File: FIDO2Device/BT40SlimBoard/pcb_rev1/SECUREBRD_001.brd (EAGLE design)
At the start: 30 x 30 mm, 31 parts, among them CN1 2137160001, CN2 IF_5PIN_H, CN3 IF_4PIN_SOL, SW1 SKRPACE010, SW2 SKRPACE010, SW3 SKTADAE010, U1 BT40, U2 ADP122ACPZ-3.3-R7

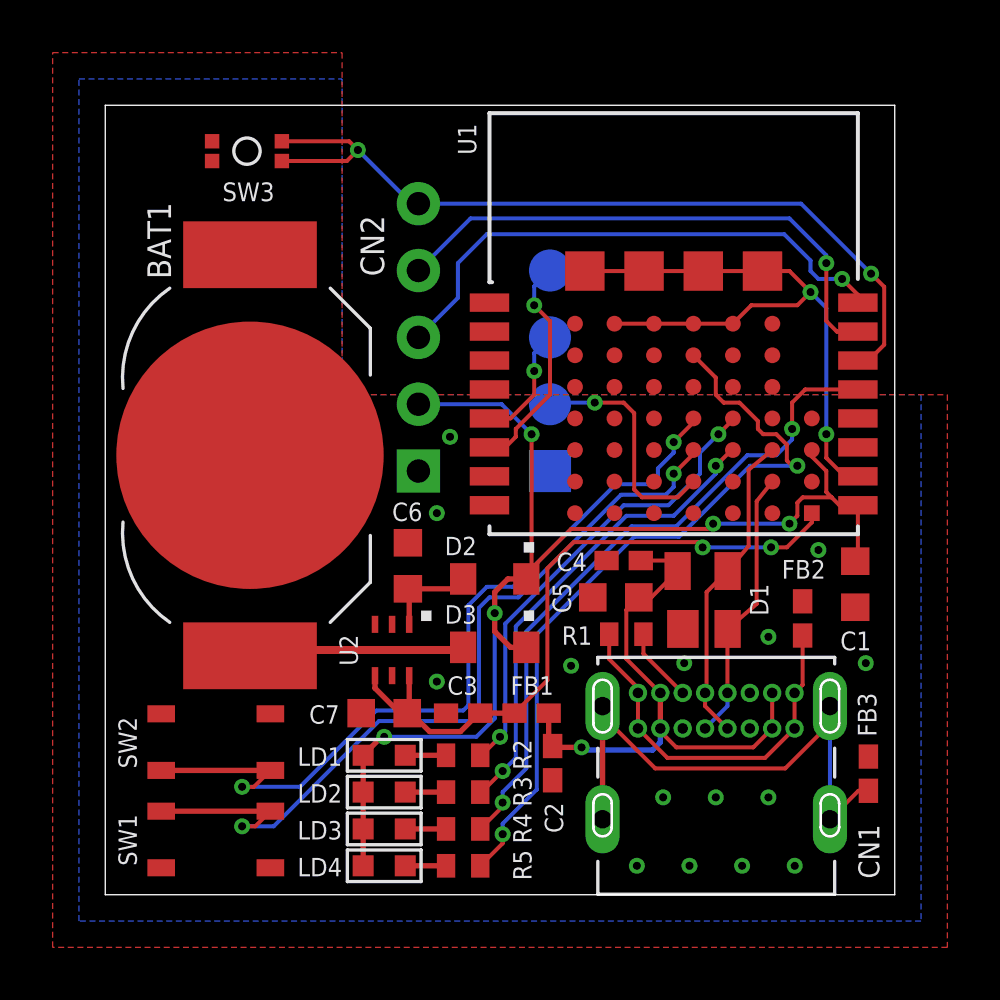
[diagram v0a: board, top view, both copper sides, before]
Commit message: パターンの改善
・裏面べたGNDの狭かった経路部分を拡張
（スイッチ、LEDのviaを改善）
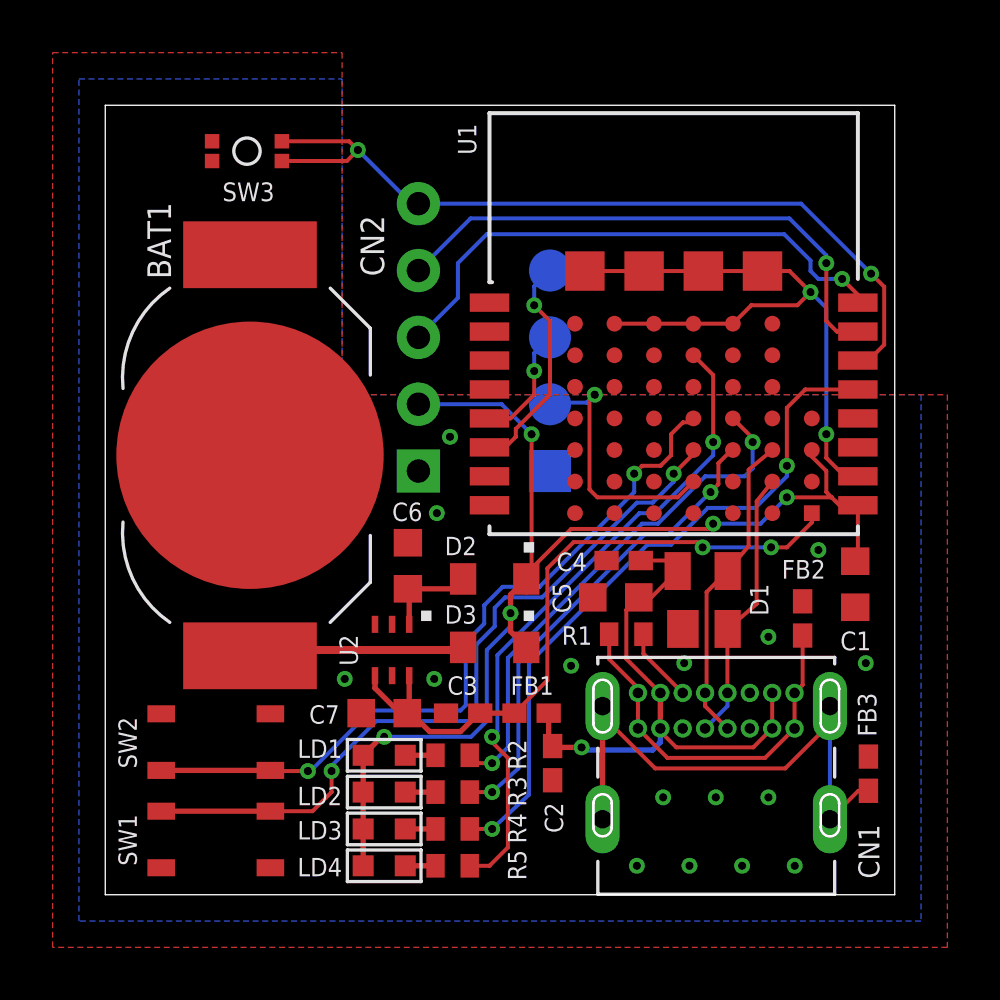
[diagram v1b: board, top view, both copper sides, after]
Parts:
- moved R2 0.40 mm to (13.2, 5.30)
- moved R3 0.40 mm to (13.2, 3.90)
- moved R4 0.40 mm to (13.2, 2.50)
- moved R5 0.40 mm to (13.2, 1.10)
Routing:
- net LED4: track 28.8 -> 24.8 mm
- net SW1: track 31.3 -> 28.7 mm
- net SW2: track 31.2 -> 28.6 mm
- net LED1: track 17.8 -> 19.8 mm
- net VDD_NRF: track 48.0 -> 46.6 mm
- net TXD: track 8.91 -> 9.85 mm
- net LED3: track 25.5 -> 26.1 mm
- net 0V: vias 17 -> 18
